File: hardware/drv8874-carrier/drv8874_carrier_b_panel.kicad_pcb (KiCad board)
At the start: 2 copper layers, 45.7 x 45.6 mm, 73 parts, among them J1_1 1x7 0.1in pins (hand-soldered), J1_2 1x7 0.1in pins (hand-soldered), J1_3 1x7 0.1in pins (hand-soldered), J1_4 1x7 0.1in pins (hand-soldered), J1_5 1x7 0.1in pins (hand-soldered), J1_6 1x7 0.1in pins (hand-soldered), J2_1 1x7 0.1in pins (hand-soldered), J2_2 1x7 0.1in pins (hand-soldered), J2_3 1x7 0.1in pins (hand-soldered), J2_4 1x7 0.1in pins (hand-soldered), J2_5 1x7 0.1in pins (hand-soldered), J2_6 1x7 0.1in pins (hand-soldered), U1_1 DRV8874PWPR, U1_2 DRV8874PWPR, U1_3 DRV8874PWPR, U1_4 DRV8874PWPR, U1_5 DRV8874PWPR, U1_6 DRV8874PWPR

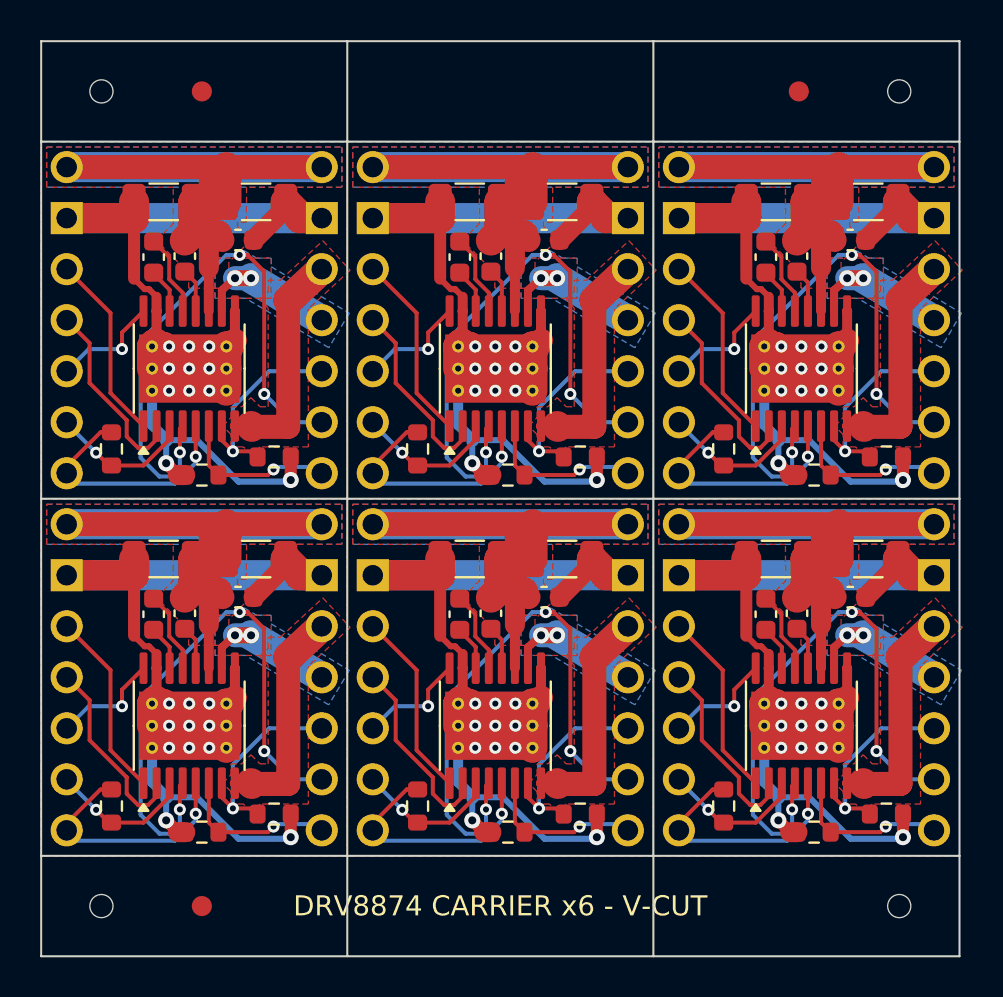
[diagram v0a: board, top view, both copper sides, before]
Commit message: DRV8874 carrier: Basic parts only besides the DRV8874, add C4
- C1, C2: 10 uF 25 V 0805 (C15850) instead of 50 V 1206 (C13585), much
  cheaper.
- C5: 22 nF 0402 (C1532, Basic) instead of 0603 (C77571, Extended).
- R3: 2.4 k (C22940, Basic) instead of 2.49 k. CS reads 1.08 V/A and the
  driver limit is about 3.1 A.
- C4: second 100 nF on VM, by the VM header pin, as on Pololu's board.
- A no-tracks rule area keeps signals from under U1 on B.Cu, so the
  thermal pad's bottom pour is unbroken. Version B now gets all 15
  thermal vias.
- R3's GND pad gets its own via. GND is no longer widened (it is poured).

Firmware: the driver choice is now a menuconfig choice between this
carrier (default, 1.08 V/A), Pololu #4035 (1.12 V/A) and #4036
(2.49 V/A). Host tests pass for all three.
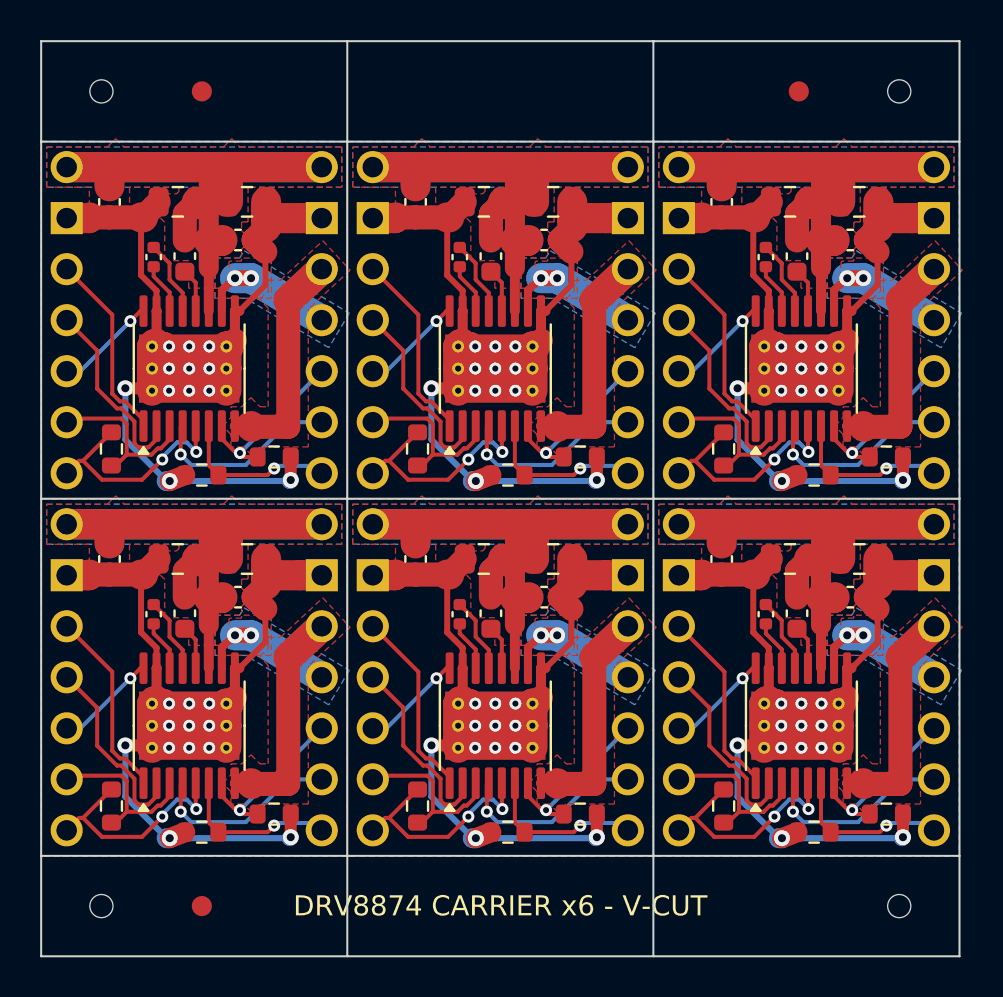
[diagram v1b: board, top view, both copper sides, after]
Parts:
- added C4_1: 100nF 50V, C_0603_1608Metric, F.Cu at (103.4, 108.0)
- added C4_2: 100nF 50V, C_0603_1608Metric, F.Cu at (118.6, 108.0)
- added C4_3: 100nF 50V, C_0603_1608Metric, F.Cu at (133.9, 108.0)
- added C4_4: 100nF 50V, C_0603_1608Metric, F.Cu at (103.4, 125.8)
- added C4_5: 100nF 50V, C_0603_1608Metric, F.Cu at (118.6, 125.8)
- added C4_6: 100nF 50V, C_0603_1608Metric, F.Cu at (133.9, 125.8)
- C1_1, C1_2, C1_3, C1_4, C1_5, C1_6, C2_1, C2_2, C2_3, C2_4, C2_5, C2_6: value 10uF 50V -> 10uF 25V; footprint C_1206_3216Metric -> C_0805_2012Metric
- C5_1, C5_2, C5_3, C5_4, C5_5, C5_6: footprint C_0603_1608Metric -> C_0402_1005Metric
- R3_1, R3_2, R3_3, R3_4, R3_5, R3_6: value 2.49k 1% -> 2.4k 1%
- moved C1_1 0.70 mm to (106.8, 108.0)
- moved C1_2 0.70 mm to (122.0, 108.0)
- moved C1_4 0.70 mm to (106.8, 125.8)
- moved C1_5 0.70 mm to (122.0, 125.8)
- moved C1_3 0.70 mm to (137.3, 108.0)
- moved C1_6 0.70 mm to (137.3, 125.8)
- moved C2_3 0.45 mm to (140.7, 108.0)
- moved C2_6 0.45 mm to (140.7, 125.8)
- moved C2_1 0.45 mm to (110.2, 108.0)
- moved C2_2 0.45 mm to (125.5, 108.0)
- moved C2_4 0.45 mm to (110.2, 125.8)
- moved C2_5 0.45 mm to (125.5, 125.8)
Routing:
- net FAULT: track 169.8 -> 57.5 mm, vias 18 -> 6
- net GND: track 326.0 -> 279.9 mm, vias 66 -> 72
- net IMODE: track 61.1 -> 51.3 mm
- net SLEEP: track 43.5 -> 52.8 mm, vias 6 -> 0
- net VM: track 227.7 -> 233.8 mm
- net VREF: track 73.1 -> 68.6 mm, vias 6 -> 12
- net PMODE: track 33.3 -> 30.4 mm
- net CPL: track 13.5 -> 15.2 mm
- net CPH: track 24.4 -> 22.6 mm
- net EN: track 56.4 -> 57.3 mm
